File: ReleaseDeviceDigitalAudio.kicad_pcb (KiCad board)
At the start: 4 copper layers, 132 x 68.5 mm, 179 parts, among them J1 Conn_02x10_Counter_Clockwise, J2 ATMEGA_PROG, J3 SignalStrength, J4 UIBoardCON1, J5 Conn_01x04, J6 UIBoardCON2, J7 KeySwitch, Q1 BSS314PEH6327XTSA1, Q3 SQ2362ES-T1_GE3, Q4 SQD50P06-15L_GE3, U1 ATmega4809-A, U10 ULN2003F12FN-7, U11 ULN2003F12FN-7, U12 ULN2003F12FN-7, U13 ULN2003F12FN-7, U14 MAX98089ETN+, U15 SN74LV1T126, U16 SN74LV1T126, U17 BM83SM1-00TA, U18 PCF85063A, U2 VOMA617A, U3 VOMA617A, U4 LM53635LQRNL*Q1, U5 TLVH431AQDBVRQ1, U6 LM74610-Q1, U7 Compute_Module_4_Connectors, U8 CD4514BM, U9 CD4511BPWR, Y1 9HT12

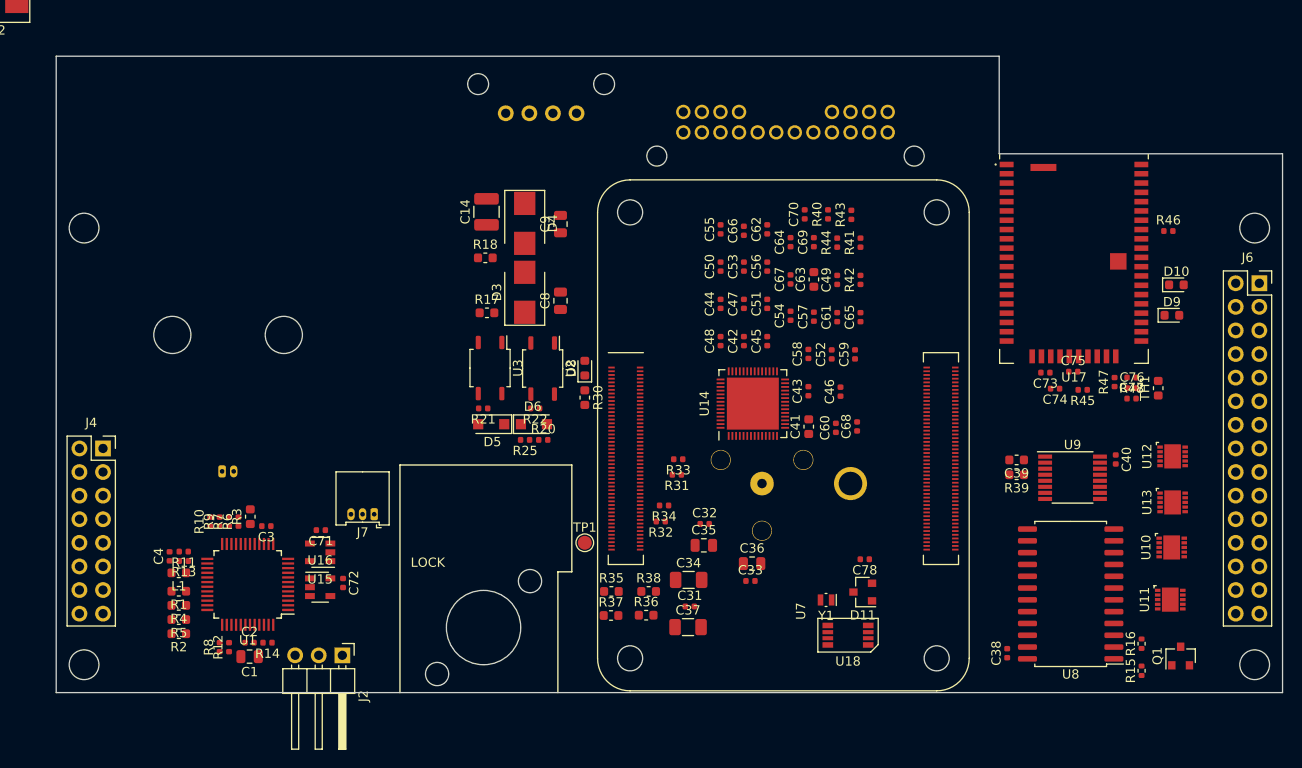
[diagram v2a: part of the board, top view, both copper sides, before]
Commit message: - Layout Zwischenstand, UI Board Ansteuerung fast fertig - GPIOs von ATmega komplett umsortiert - Darlington Anschlüsse umsortiert
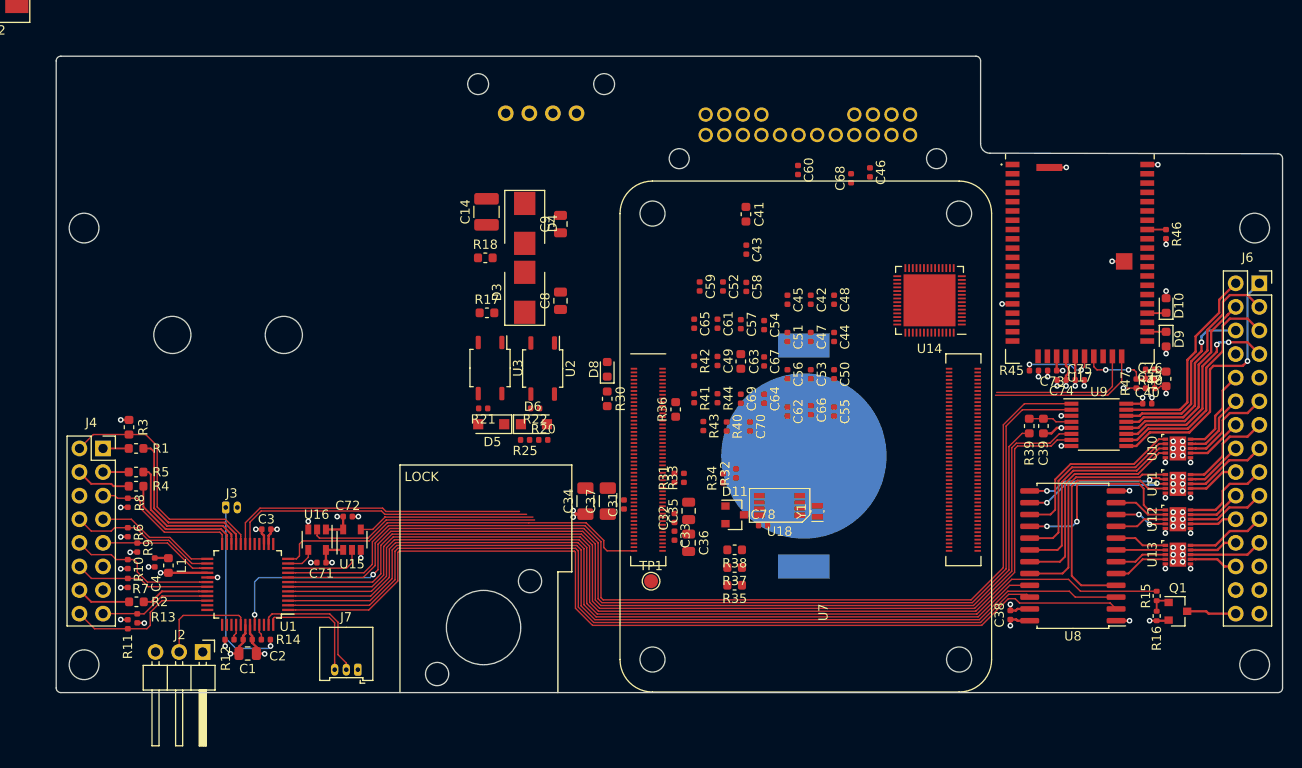
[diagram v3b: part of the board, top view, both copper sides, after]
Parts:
- BT1: footprint TeKaDeConn:CR1220 -> Battery:BatteryHolder_MPD_BC2003_1x2032
- moved C60 28.1 mm to (163.8, 73.2), turned to 270 degrees
- moved R43 27.8 mm to (153.7, 100.8), turned to 270 degrees
- moved C68 26.7 mm to (169.6, 74.1)
- moved R40 25.3 mm to (156.2, 100.9), turned to 270 degrees
- moved R41 24.5 mm to (152.7, 97.8), turned to 270 degrees
- moved C41 23.8 mm to (158.2, 78.0), turned to 270 degrees
- moved C46 23.8 mm to (171.6, 73.5), turned to 270 degrees
- moved C70 23.6 mm to (158.7, 100.9), turned to 270 degrees
- moved C55 23.1 mm to (167.7, 99.2), turned to 270 degrees
- moved R36 22.4 mm to (150.7, 99.0), turned to 90 degrees
- moved U14 22.0 mm to (178.0, 87.3), turned to 180 degrees
- moved R44 21.1 mm to (155.2, 97.8), turned to 270 degrees
- moved C66 20.6 mm to (165.2, 99.1), turned to 270 degrees
- moved R42 19.9 mm to (152.7, 93.8), turned to 270 degrees
- moved C62 19.7 mm to (162.7, 99.2), turned to 270 degrees
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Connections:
- net Net-(R12-Pad2) renamed /ControllerUIBoard/AVRRESET
- J7 pad 1: /ControllerUIBoard/KeySwitchA -> GND
- J7 pad 3: GND -> /ControllerUIBoard/KeySwitchA
- R11 pad 1: /ControllerUIBoard/DataEncoderDataOutD -> /ControllerUIBoard/DataEncoderDataOutE
- R13 pad 1: /ControllerUIBoard/DataEncoderDataOutE -> /ControllerUIBoard/DataEncoderDataOutD
- R4 pad 2: /ControllerUIBoard/LED_RD -> /ControllerUIBoard/LED_GN
- R5 pad 2: /ControllerUIBoard/LED_GN -> /ControllerUIBoard/LED_RD
- U1 pad 1: Net-(R15-Pad2) -> /7SegmentDriver/7Seg_Decoder_D1
- U1 pad 12: Net-(U1-Pad12) -> /ControllerUIBoard/RPI_RUN
- U1 pad 16: /7SegmentDriver/7Seg_Decoder_D1 -> Net-(U1-Pad16)
- U1 pad 17: /7SegmentDriver/7Seg_Decoder_D2 -> Net-(U1-Pad17)
- U1 pad 18: /7SegmentDriver/7Seg_Decoder_D3 -> /ControllerUIBoard/IGNITION_SENSE
- U1 pad 19: /7SegmentDriver/7Seg_Decoder_D4 -> /ControllerUIBoard/5V_EN_OUT
- U1 pad 2: Net-(U1-Pad2) -> /7SegmentDriver/7Seg_Decoder_D4
- U1 pad 21: /ControllerUIBoard/DataEncoderDataAvailable -> Net-(R1-Pad1)
- U1 pad 22: /ControllerUIBoard/DataEncoderDataOutA -> Net-(R5-Pad1)
- U1 pad 23: /ControllerUIBoard/DataEncoderDataOutB -> Net-(R4-Pad1)
- U1 pad 24: /ControllerUIBoard/DataEncoderDataOutC -> /ControllerUIBoard/ButtonA2GND
- U1 pad 25: /ControllerUIBoard/DataEncoderDataOutD -> /ControllerUIBoard/DataEncoderOutputEnable
- U1 pad 26: /ControllerUIBoard/DataEncoderDataOutE -> /ControllerUIBoard/DataEncoderDataAvailable
- U1 pad 27: /ControllerUIBoard/DataEncoderOutputEnable -> /ControllerUIBoard/DataEncoderDataOutB
- U1 pad 3: Net-(U1-Pad3) -> /7SegmentDriver/7Seg_Decoder_D2
- U1 pad 30: /7SegmentDriver/7Seg_Driver_A -> /ControllerUIBoard/DataEncoderDataOutC
- U1 pad 31: /7SegmentDriver/7Seg_Driver_B -> /ControllerUIBoard/DataEncoderDataOutA
- U1 pad 32: /7SegmentDriver/7Seg_Driver_C -> Net-(R2-Pad1)
- U1 pad 33: /7SegmentDriver/7Seg_Driver_D -> /ControllerUIBoard/DataEncoderDataOutD
- U1 pad 34: Net-(R1-Pad1) -> /ControllerUIBoard/DataEncoderDataOutE
- U1 pad 35: Net-(R4-Pad1) -> Net-(U1-Pad35)
- U1 pad 36: Net-(R5-Pad1) -> Net-(U1-Pad36)
- U1 pad 37: Net-(R2-Pad1) -> Net-(U1-Pad37)
- U1 pad 39: /ControllerUIBoard/ButtonA2GND -> Net-(U1-Pad39)
- U1 pad 4: /ControllerUIBoard/RPI_RUN -> /7SegmentDriver/7Seg_Decoder_D3
- U1 pad 47: Net-(U1-Pad47) -> /ControllerUIBoard/KeySwitchB
- U1 pad 48: Net-(U1-Pad48) -> /ControllerUIBoard/KeySwitchA
- U1 pad 5: /ControllerUIBoard/IGNITION_SENSE -> Net-(R15-Pad2)
- U1 pad 6: /ControllerUIBoard/5V_EN_OUT -> /7SegmentDriver/7Seg_Driver_A
- U1 pad 7: /ControllerUIBoard/KeySwitchA -> /7SegmentDriver/7Seg_Driver_D
- U1 pad 8: /ControllerUIBoard/KeySwitchB -> /7SegmentDriver/7Seg_Driver_C
- U1 pad 9: Net-(U1-Pad9) -> /7SegmentDriver/7Seg_Driver_B
- U10 pad 1: /7SegmentDriver/CathodeDigitASignal -> /7SegmentDriver/CathodeDigit14Signal
- U10 pad 10: /7SegmentDriver/CathodeDigitA -> /7SegmentDriver/CathodeDigit14
- U10 pad 2: /7SegmentDriver/CathodeDigitBSignal -> /7SegmentDriver/CathodeDigit8Signal
- U10 pad 3: /7SegmentDriver/CathodeDigit1Signal -> /7SegmentDriver/CathodeDigit7Signal
- U10 pad 4: /7SegmentDriver/CathodeDigit2Signal -> /7SegmentDriver/CathodeDigit10Signal
- U10 pad 7: /7SegmentDriver/CathodeDigit2 -> /7SegmentDriver/CathodeDigit10
- U10 pad 8: /7SegmentDriver/CathodeDigit1 -> /7SegmentDriver/CathodeDigit7
- U10 pad 9: /7SegmentDriver/CathodeDigitB -> /7SegmentDriver/CathodeDigit8
- U11 pad 1: /7SegmentDriver/CathodeDigit3Signal -> /7SegmentDriver/CathodeDigit9Signal
- U11 pad 10: /7SegmentDriver/CathodeDigit3 -> /7SegmentDriver/CathodeDigit9
- U11 pad 2: /7SegmentDriver/CathodeDigit4Signal -> /7SegmentDriver/CathodeDigit12Signal
- U11 pad 3: /7SegmentDriver/CathodeDigit5Signal -> /7SegmentDriver/CathodeDigit11Signal
- U11 pad 8: /7SegmentDriver/CathodeDigit5 -> /7SegmentDriver/CathodeDigit11
- U11 pad 9: /7SegmentDriver/CathodeDigit4 -> /7SegmentDriver/CathodeDigit12
- U12 pad 1: /7SegmentDriver/CathodeDigit7Signal -> /7SegmentDriver/CathodeDigit13Signal
- U12 pad 10: /7SegmentDriver/CathodeDigit7 -> /7SegmentDriver/CathodeDigit13
- U12 pad 2: /7SegmentDriver/CathodeDigit8Signal -> /7SegmentDriver/CathodeDigitASignal
- U12 pad 3: /7SegmentDriver/CathodeDigit9Signal -> /7SegmentDriver/CathodeDigitBSignal
- U12 pad 4: /7SegmentDriver/CathodeDigit10Signal -> /7SegmentDriver/CathodeDigit1Signal
- U12 pad 7: /7SegmentDriver/CathodeDigit10 -> /7SegmentDriver/CathodeDigit1
- U12 pad 8: /7SegmentDriver/CathodeDigit9 -> /7SegmentDriver/CathodeDigitB
- U12 pad 9: /7SegmentDriver/CathodeDigit8 -> /7SegmentDriver/CathodeDigitA
- U13 pad 1: /7SegmentDriver/CathodeDigit11Signal -> /7SegmentDriver/CathodeDigit2Signal
- U13 pad 10: /7SegmentDriver/CathodeDigit11 -> /7SegmentDriver/CathodeDigit2
- U13 pad 2: /7SegmentDriver/CathodeDigit12Signal -> /7SegmentDriver/CathodeDigit3Signal
- U13 pad 3: /7SegmentDriver/CathodeDigit13Signal -> /7SegmentDriver/CathodeDigit4Signal
- U13 pad 4: /7SegmentDriver/CathodeDigit14Signal -> /7SegmentDriver/CathodeDigit5Signal
- U13 pad 7: /7SegmentDriver/CathodeDigit14 -> /7SegmentDriver/CathodeDigit5
- U13 pad 8: /7SegmentDriver/CathodeDigit13 -> /7SegmentDriver/CathodeDigit4
- U13 pad 9: /7SegmentDriver/CathodeDigit12 -> /7SegmentDriver/CathodeDigit3
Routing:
- net /7SegmentDriver/BrightnessPWM: track 0.00 -> 114.2 mm, vias 0 -> 2
- net /7SegmentDriver/7Seg_Driver_B: track 0.00 -> 112.4 mm
- net /7SegmentDriver/7Seg_Driver_C: track 0.00 -> 112.4 mm
- net /7SegmentDriver/7Seg_Driver_D: track 0.00 -> 110.7 mm
- net /7SegmentDriver/7Seg_Driver_A: track 0.00 -> 110.6 mm
- net Net-(R15-Pad2): track 0.00 -> 106.5 mm
- net /7SegmentDriver/7Seg_Decoder_D1: track 0.00 -> 102.0 mm
- net /7SegmentDriver/7Seg_Decoder_D2: track 0.00 -> 101.8 mm
- net /7SegmentDriver/7Seg_Decoder_D4: track 0.00 -> 92.4 mm
- net /7SegmentDriver/7Seg_Decoder_D3: track 0.00 -> 92.3 mm
- net /ControllerUIBoard/RPI_RUN: track 0.00 -> 41.3 mm
- net GND: track 0.00 -> 39.2 mm, vias 0 -> 57
- net /ControllerUIBoard/IGNITION_SENSE: track 0.00 -> 32.8 mm
- net /ControllerUIBoard/5V_EN_OUT: track 0.00 -> 32.6 mm
- net +5V: track 0.00 -> 31.8 mm, vias 0 -> 17
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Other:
- outline, holes or cut-outs redrawn
- net class Default: trace_width 0.2032 -> 0.1524

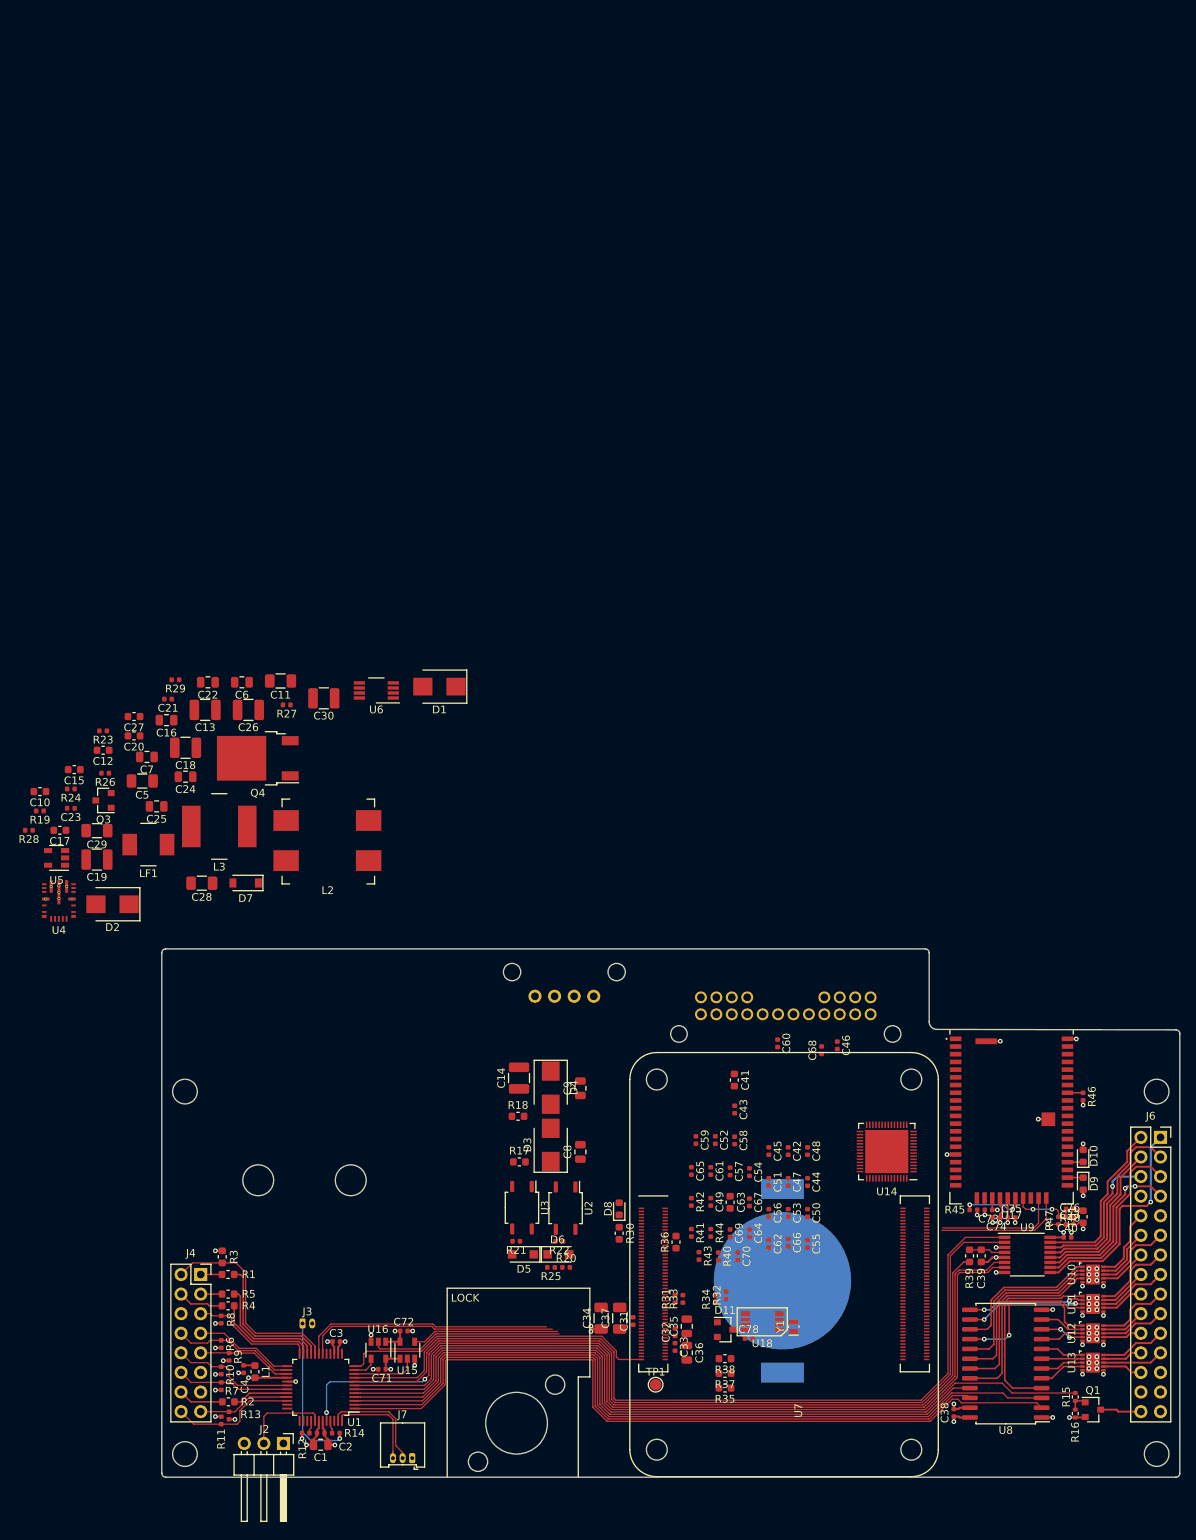
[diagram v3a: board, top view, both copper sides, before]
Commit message: - BT1 fixed
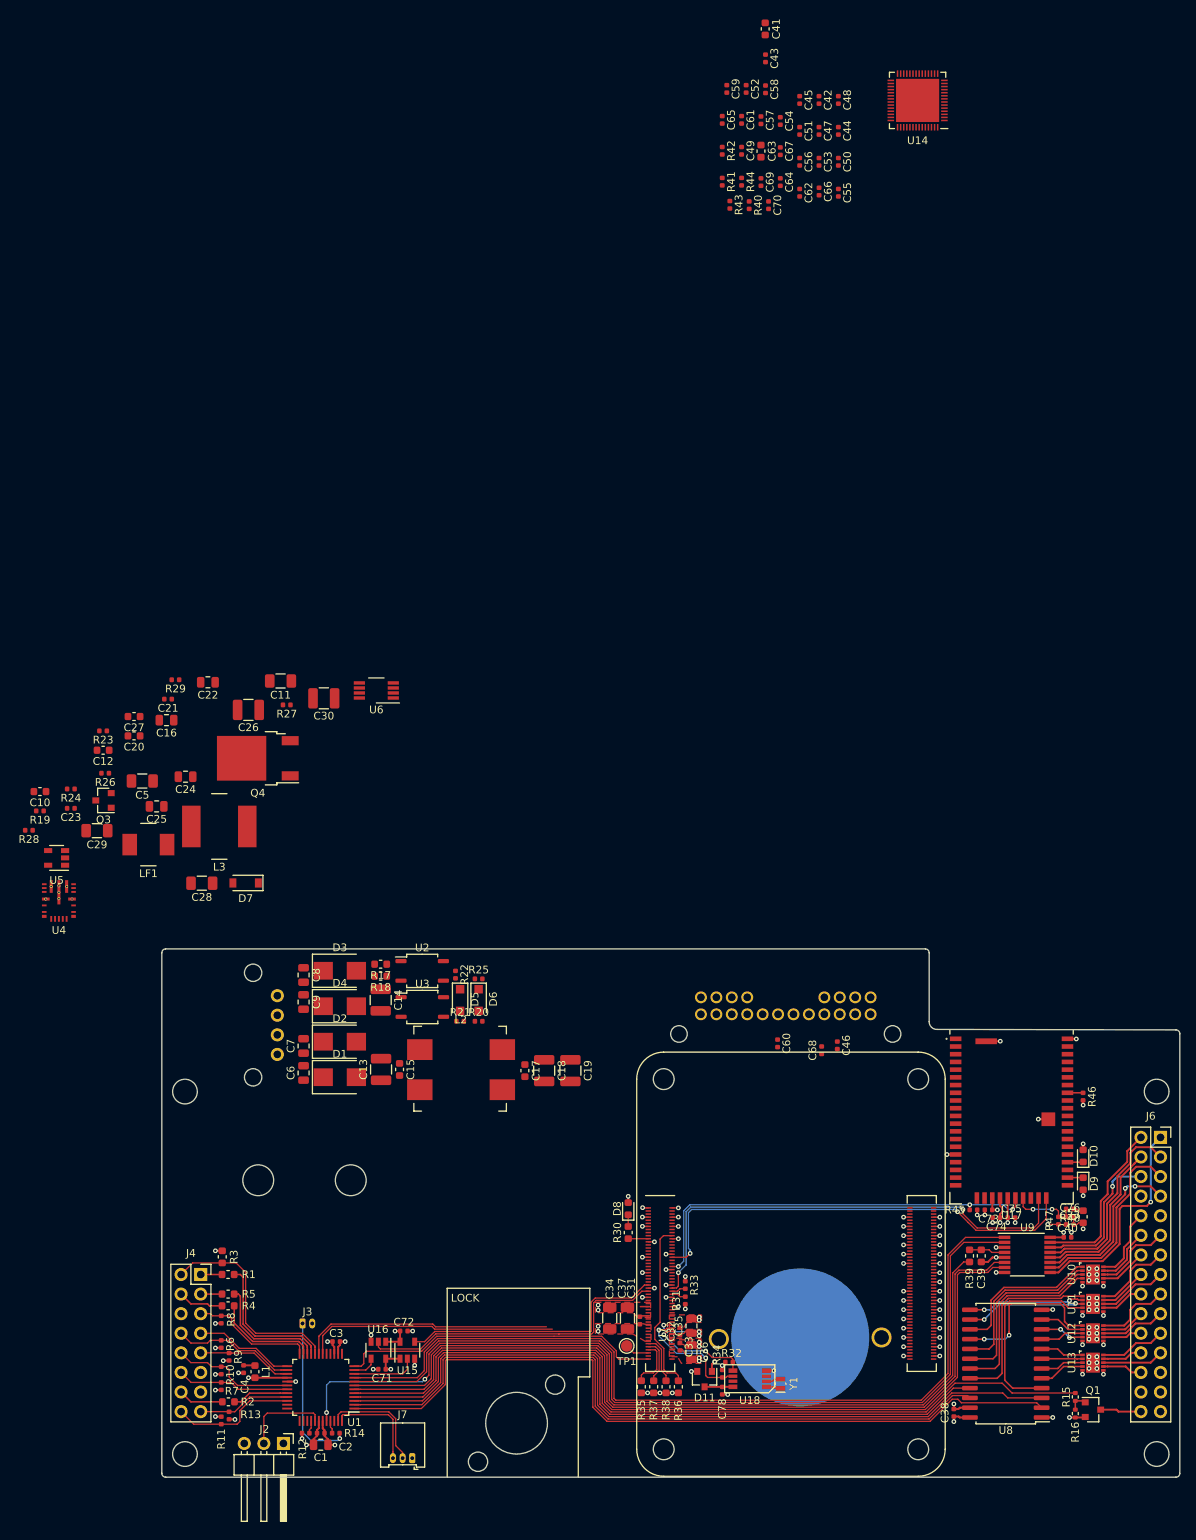
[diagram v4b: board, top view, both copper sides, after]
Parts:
- BT1: footprint Battery:BatteryHolder_MPD_BC2003_1x2032 -> TeKaDe:BAT-HLD-005-THM
- moved C41 136.4 mm to (162.2, -58.3)
- moved C42 136.4 mm to (169.2, -49.1)
- moved C43 136.4 mm to (162.3, -54.5)
- moved C44 136.4 mm to (171.7, -45.1)
- moved C45 136.4 mm to (166.7, -49.1)
- moved C47 136.4 mm to (169.2, -45.1)
- moved C48 136.4 mm to (171.7, -49.1)
- moved C49 136.4 mm to (159.2, -42.5)
- moved C50 136.4 mm to (171.7, -41.1)
- moved C51 136.4 mm to (166.7, -45.1)
- moved C52 136.4 mm to (159.8, -50.5)
- moved C53 136.4 mm to (169.2, -41.1)
- moved C54 136.4 mm to (164.2, -46.4)
- moved C56 136.4 mm to (166.7, -41.1)
- moved C57 136.4 mm to (161.7, -46.5)
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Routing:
- net GND: track 39.2 -> 85.5 mm, vias 57 -> 115
- net /RPiCM4/UART3_TX: track 16.0 -> 61.9 mm, vias 0 -> 2
- net /BluetoothModule/BM83_MFB: track 8.12 -> 53.9 mm, vias 2 -> 3
- net /RPiCM4/UART3_RX: track 16.9 -> 58.9 mm, vias 0 -> 2
- net +3V3: track 6.11 -> 31.5 mm, vias 2 -> 10
- net /RPiCM4/EEPROM_nWP: track 0.00 -> 22.3 mm
- net /RPiCM4/UART0_RX: track 19.1 -> 35.5 mm
- net /RPiCM4/UART0_TX: track 25.0 -> 41.1 mm
- net /RPiCM4/I2C0_SCL: track 0.00 -> 15.8 mm, vias 0 -> 2
- net /RPiCM4/I2C0_SDA: track 0.00 -> 13.0 mm, vias 0 -> 2
- net /RPiCM4/nRPIBOOT: track 0.00 -> 6.56 mm
- net /RPiCM4/WL_nDisable: track 0.00 -> 6.33 mm
- net /RPiCM4/BT_nDisable: track 0.00 -> 5.83 mm
- net Net-(BT1-Pad1): track 0.00 -> 4.57 mm, vias 0 -> 1
- net Net-(C78-Pad1): track 0.00 -> 3.69 mm
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- added copper zone on F.Cu, net +1V8
- added copper zone on F.Cu, net +3V3
- added copper zone on In2.Cu, net +3V3
- added copper zone on F.Cu, net +5V
- added copper zone on F.Cu, net GND
